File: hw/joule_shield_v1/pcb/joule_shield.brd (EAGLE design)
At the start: 60 x 40 mm, 138 parts, among them J1 MF-CON-MICROUSB-RIGHT, J4 USB_AUSB_A_SMT_RA, J5 JST-ZH5JST_ZH_SMT_VERT, J6 INTEL_JOULE_J6, J7 INTEL_JOULE_J7, J8 DM3ATDM3AT, SW1 MF-SW-TACT-4.2MM, SW2 MF-SW-TACT-4.2MM, SW3 MF-SW-TACT-4.2MM, U1 BQ25892PWQFN-24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

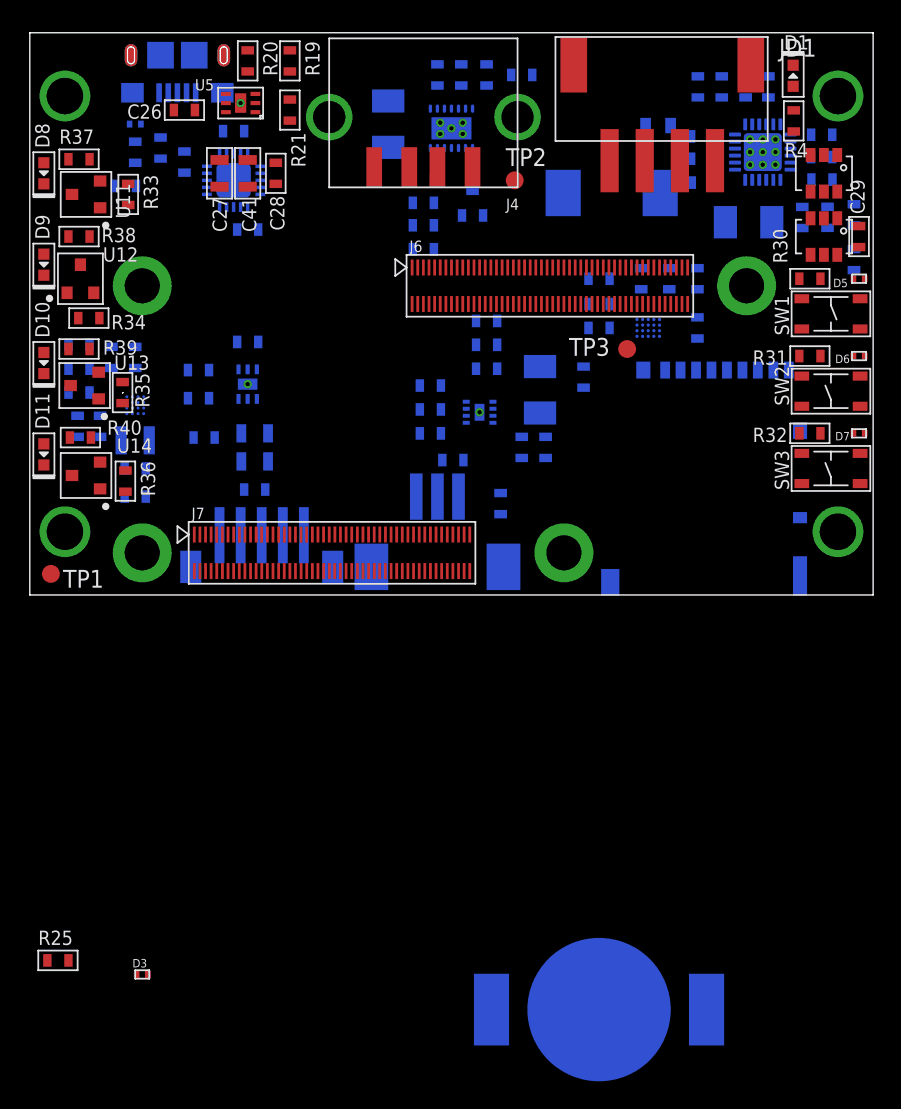
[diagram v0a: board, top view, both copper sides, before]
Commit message: joule shield: Put a sufficient keepout distance around m2.5 mounting holes.
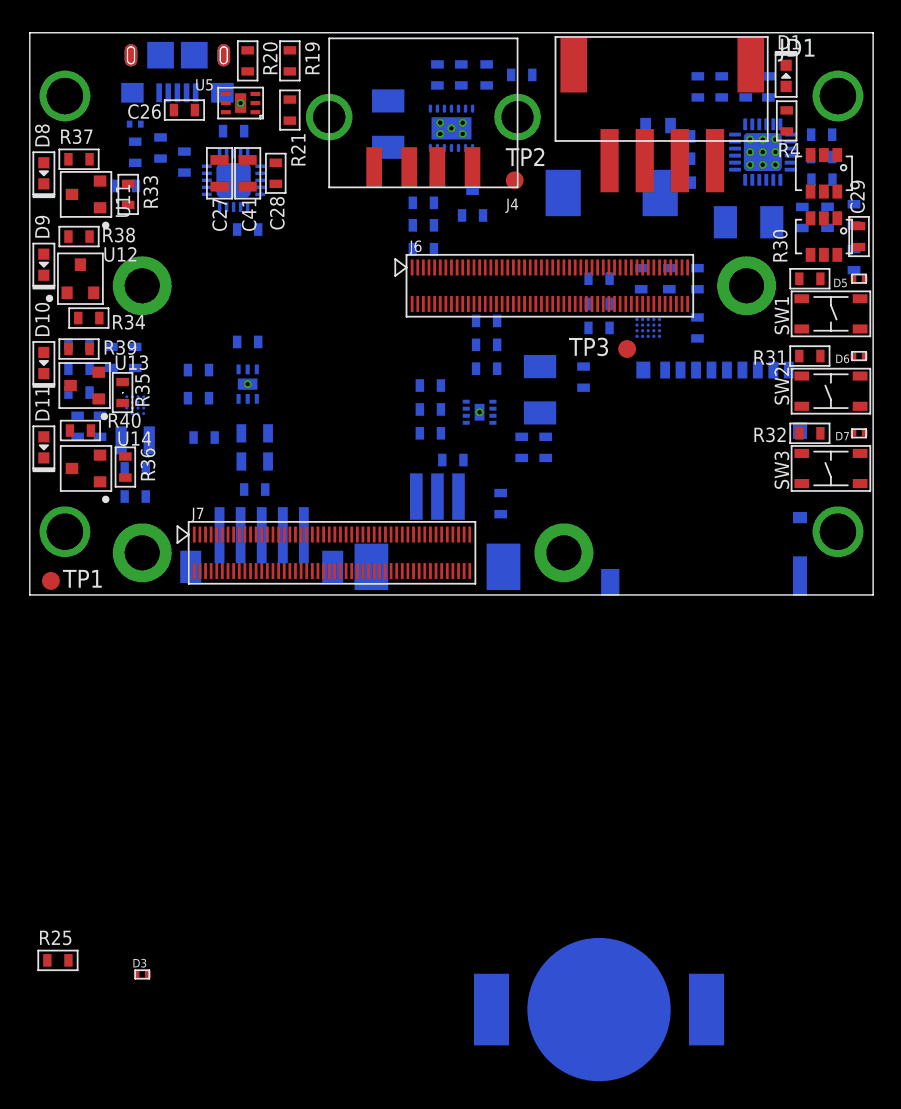
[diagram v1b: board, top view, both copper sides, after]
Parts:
- moved R36 1.00 mm to (6.80, 9.10)
- moved D1 0.50 mm to (53.8, 36.9)
- moved D11 0.50 mm to (1.00, 10.5)
- moved R4 0.50 mm to (53.9, 33.7)
- moved R40 0.50 mm to (3.60, 11.7)
- moved TP1 0.50 mm to (1.50, 1.00)
- moved U14 0.50 mm to (4.00, 9.00)
- flipped U$54 to the top

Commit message: joule shield: Switch to a smaller RTC battery and get everything on the board.
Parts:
- JRTC: value BK-916BK-916 -> BC-2009; device joule_shield:BK-916 -> joule_shield:BC-2009
- moved JRTC 53.9 mm to (19.2, 20.0), turned to 0 degrees
- moved D3 43.5 mm to (9.50, 16.5), flipped to the bottom, turned to 180 degrees
- moved R25 41.7 mm to (12.0, 14.5), flipped to the bottom, turned to 270 degrees
- moved C32 8.25 mm to (24.0, 9.50), turned to 270 degrees
- moved C30 8.14 mm to (10.0, 12.0), turned to 270 degrees
- moved R23 7.50 mm to (12.0, 8.50), turned to 90 degrees
- moved C42 6.02 mm to (22.0, 9.00), turned to 270 degrees
- moved R22 5.82 mm to (13.9, 8.50), turned to 90 degrees
- moved C12 5.76 mm to (5.50, 12.4)
- moved R11 5.72 mm to (4.90, 22.0)
- moved R8 5.68 mm to (3.30, 22.0)
- moved U2 5.59 mm to (5.00, 18.5)
- moved C11 5.39 mm to (5.50, 14.0)
- moved L2 5.39 mm to (5.50, 16.0)
- moved R24 5.22 mm to (16.8, 8.40), turned to 270 degrees
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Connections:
- net GND: now also JRTC.N1; no longer JRTC.2
- net N$30: now also JRTC.P1, JRTC.P2; no longer JRTC.1, JRTC.3

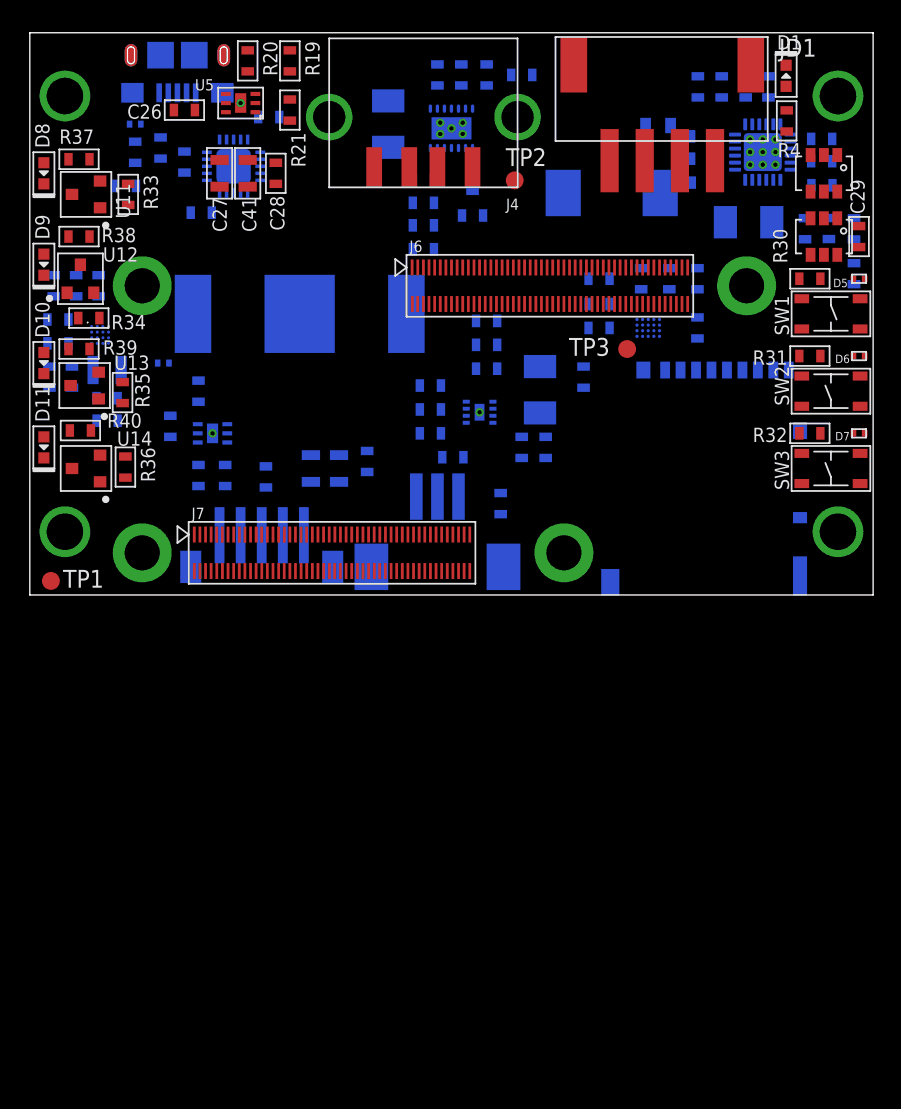
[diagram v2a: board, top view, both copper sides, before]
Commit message: joule_shield: Swap SD level converter for one with a 0.5mm BGA pitch so that there is at least one macrofab process which can route it. Further work on draft placement.  Everything is kinda on the board now.
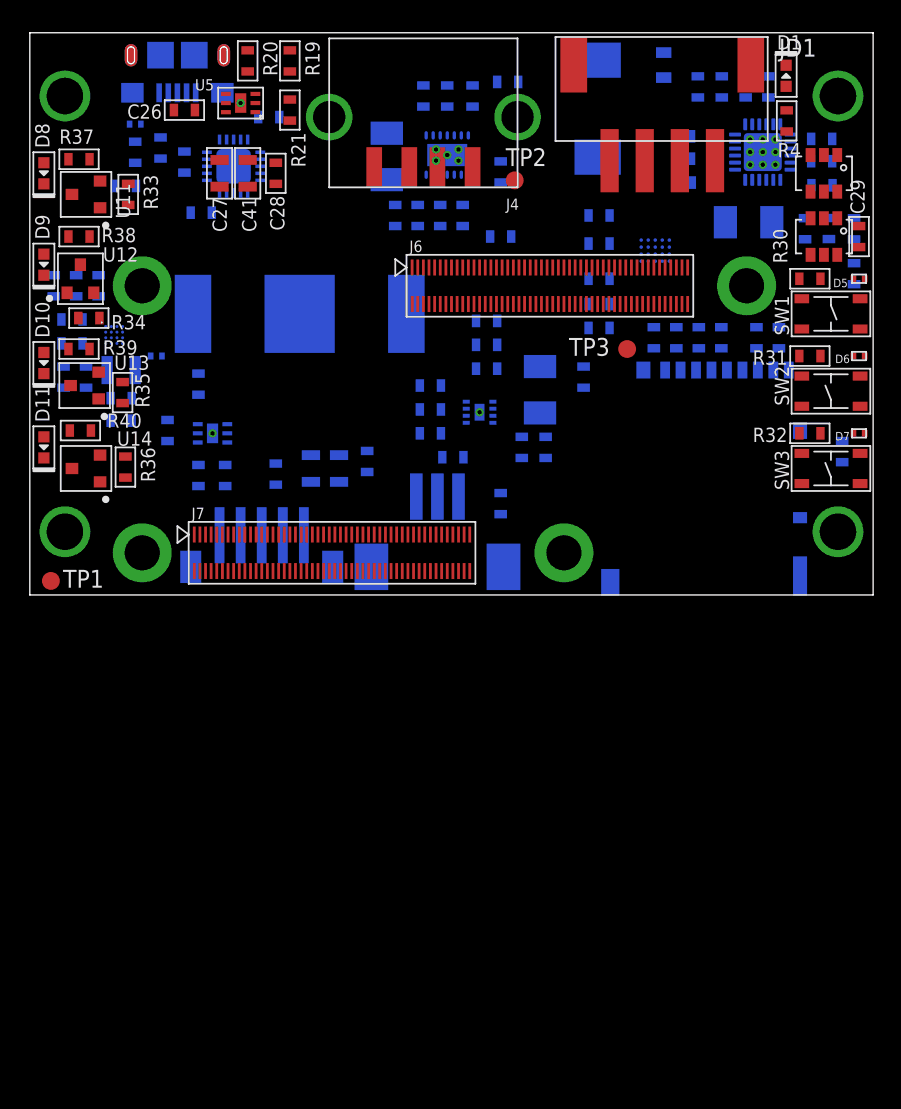
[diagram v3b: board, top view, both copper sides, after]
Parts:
- added R41, R42, R43, R44, R45: 100k, mf_passives:R0603
- U9: value TXS0206-29 -> SN74AVCA406L; device joule_shield:DSBGA20 -> joule_shield:S-PBGA-N20
- moved R26 16.0 mm to (57.8, 10.2), turned to 270 degrees
- moved C35 6.73 mm to (40.5, 27.0), turned to 0 degrees
- moved D2 6.08 mm to (40.4, 34.6), turned to 270 degrees
- moved U9 5.52 mm to (44.5, 24.5), turned to 0 degrees
- moved F1 4.32 mm to (45.1, 37.7), turned to 270 degrees
- moved FB2 3.91 mm to (40.5, 25.0), turned to 0 degrees
- moved C20 3.69 mm to (30.8, 27.0), turned to 270 degrees
- moved C17 3.20 mm to (26.0, 27.0), turned to 270 degrees
- moved R14 2.50 mm to (33.5, 25.5)
- moved L3 2.30 mm to (25.4, 31.2)
- moved C16 2.09 mm to (33.5, 30.1)
- moved U3 1.92 mm to (29.7, 31.3)
- moved C36 1.84 mm to (49.2, 18.3)
- moved C13 1.80 mm to (28.0, 35.5)
- moved C14 1.80 mm to (29.7, 35.5)
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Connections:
- removed net N$35: C36.P$1, J8.4, U9.B3
- removed net N$37: C34.P$1, C35.P$1, FB2.P$1, U9.B2
- removed net N$38: C33.P$1, FB1.P$2, U9.A2
- removed net N$40: J8.7, U9.D4
- new net N$69: J8.7, R45.P$2, U9.D2
- new net SDCARD_LVL_CMD_DIR: J6.90, U9.B5
- new net SDCARD_LVL_DAT_DIR: J6.67, U9.C1, U9.C5
- new net SDCARD_VCCA: C33.P$1, FB1.P$2, R26.P$1, U9.A5
- new net SDCARD_VCCB: C34.P$1, C35.P$1, C36.P$1, FB2.P$1, J8.4, R41.P$1, R42.P$1, R43.P$1, R44.P$1, R45.P$1, U9.D5
- net GND: now also U9.B3; no longer R26.P$2, U9.C2
- net N$41: now also R44.P$2, U9.D1; no longer U9.E4
- net N$42: now also R43.P$2, U9.C4; no longer U9.A4
- net N$43: now also R42.P$2, U9.D4; no longer U9.B4
- net N$44: now also R41.P$2, U9.C2; no longer U9.C4
- net SDCARD_CD: now also R26.P$2; no longer U9.A3
- net SDCARD_CLK: now also U9.A3; no longer U9.D2
- net SDCARD_CLK_FB: now also U9.A1; no longer U9.E2
- net SDCARD_CMD: now also U9.B1; no longer U9.C1
- net SDCARD_D0: now also U9.B2; no longer U9.D1
- net SDCARD_D1: now also U9.A2; no longer U9.E1
- net SDCARD_D2: now also U9.B4; no longer U9.A1
- net SDCARD_D3: now also U9.A4; no longer U9.B1
- net SDCARD_PWR_DOWN_N: no longer R26.P$1, U9.E3

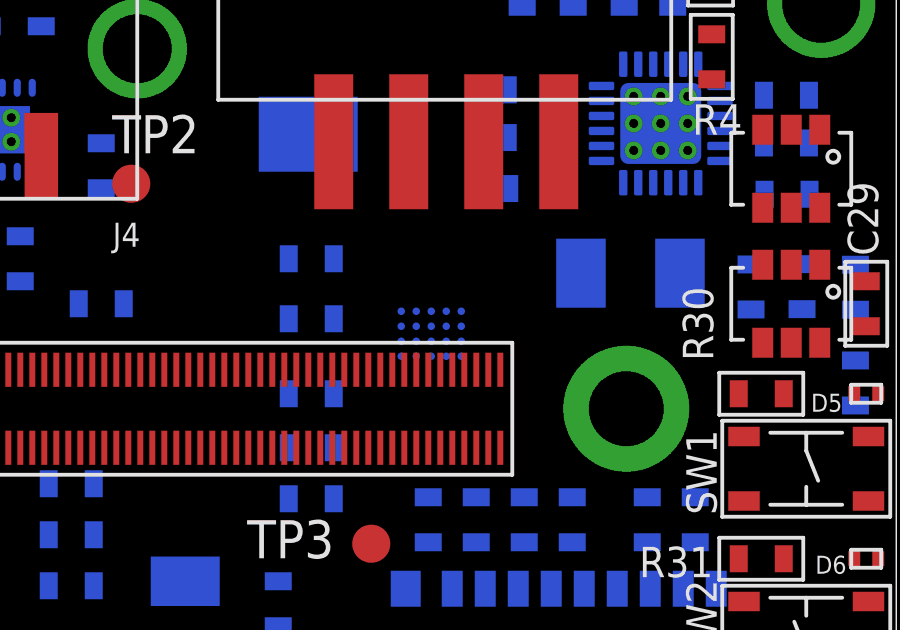
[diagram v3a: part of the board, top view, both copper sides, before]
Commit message: joule_shield: Switch to the MF extended DRU file.
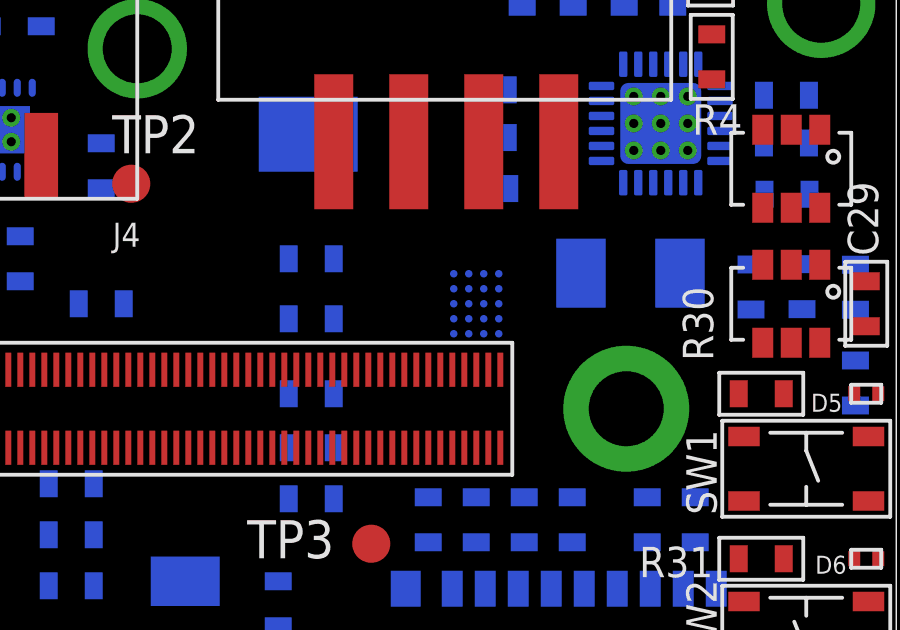
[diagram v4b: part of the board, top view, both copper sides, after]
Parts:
- moved U9 1.80 mm to (46.0, 25.5), turned to 270 degrees

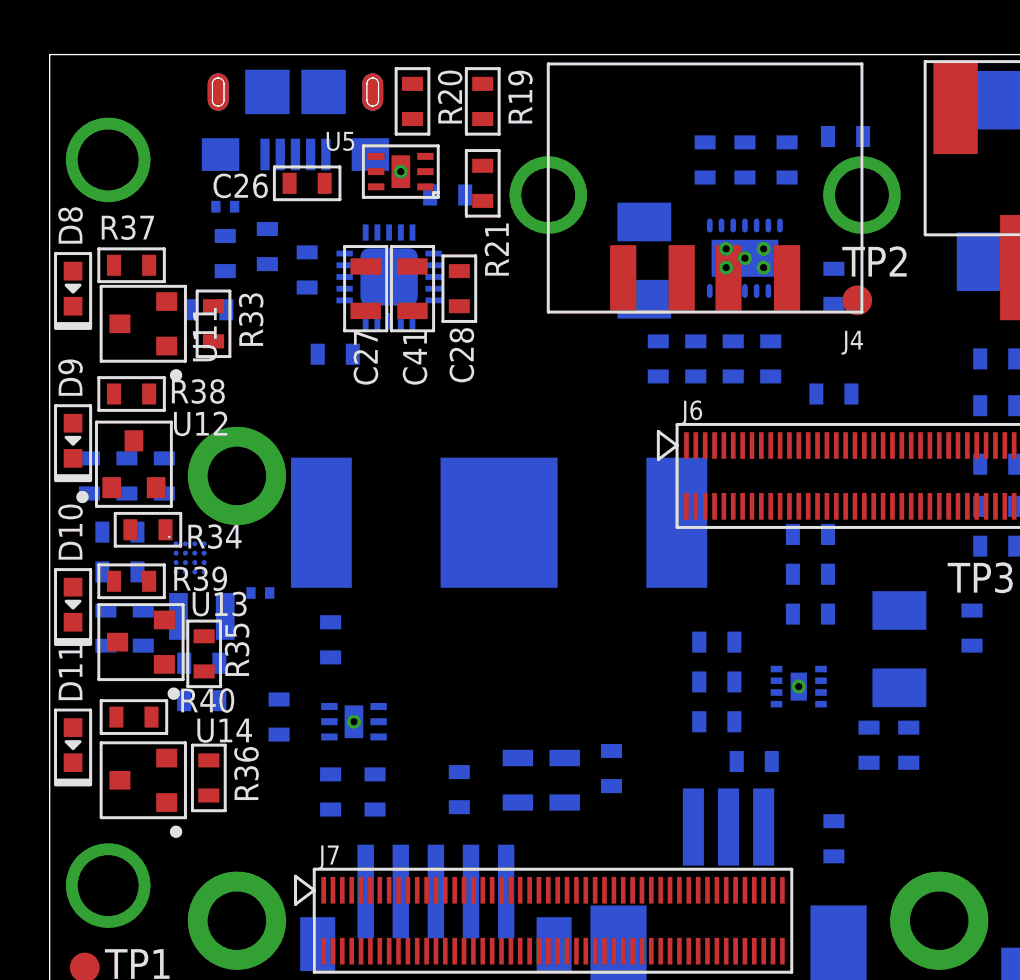
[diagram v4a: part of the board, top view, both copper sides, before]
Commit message: joule_shield: Connected up usb power switch enable and fault lines to GPIO pins.  Switched to smaller mosfets instead of MF house bipolars.
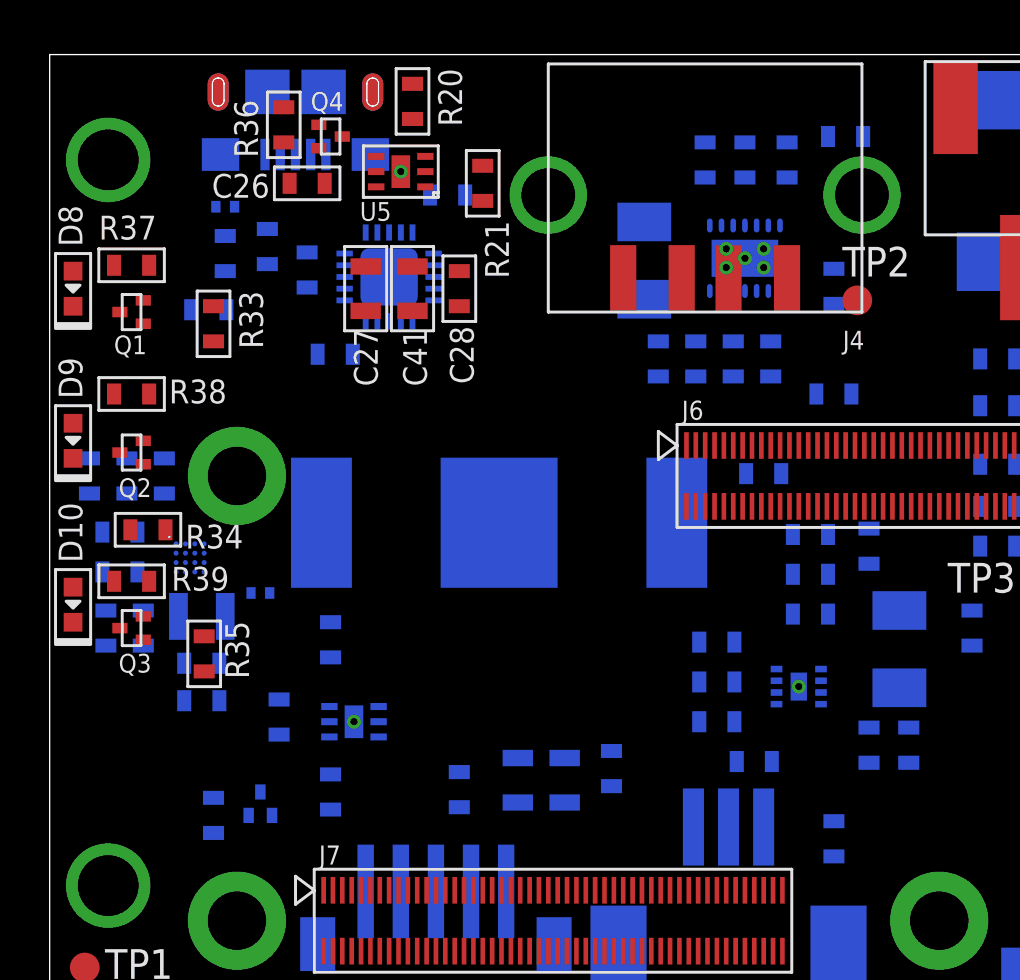
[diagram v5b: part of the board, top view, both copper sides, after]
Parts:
- removed D11: MF-LED-0603-GREEN, mf_leds:LED0603
- removed U11, U12, U13, U14: MF-DSC-SOT233-MMBT3904, mf_discrete_semiconductor:SOT-23-3
- added Q1, Q2, Q3, Q4, Q5: NFETEMT3F, joule_shield:EMT3F
- R36: value 1k -> 100k
- R40: value 470 -> 100k
- moved R36 28.1 mm to (10.0, 37.0)
- moved R19 25.2 mm to (35.0, 19.0), flipped to the bottom, turned to 90 degrees
- moved R22 21.5 mm to (30.5, 22.1), turned to 180 degrees
- moved R40 5.40 mm to (7.00, 7.50), flipped to the bottom, turned to 90 degrees
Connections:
- removed net N$22: R19.P$2, U5.3
- removed net N$32: R22.P$2, U6.3
- removed net N$55: D11.ANODE, R40.P$2
- removed net N$62: D11.CATHODE, U14.P$3
- removed net N$63: R33.P$2, U11.P$1
- removed net N$64: R34.P$2, U12.P$1
- removed net N$65: R35.P$2, U13.P$1
- removed net N$66: R36.P$2, U14.P$1
- new net ISH_GPIO_4: J6.29, Q5.1, R40.P$1
- new net ISH_GPIO_5: J6.38, R19.P$2, U5.3
- new net ISH_GPIO_6: J6.31, R22.P$2, U6.3
- net GND: now also Q1.2, Q2.2, Q3.2, Q4.2, Q5.2, R33.P$1, R34.P$1, R35.P$1, R36.P$2, R40.P$2; no longer U11.P$2, U12.P$2, U13.P$2, U14.P$2
- net ISH_GPIO_0: now also Q1.1, R33.P$2; no longer R33.P$1
- net ISH_GPIO_1: now also Q2.1, R34.P$2; no longer R34.P$1
- net ISH_GPIO_2: now also Q3.1, R35.P$2; no longer R35.P$1
- net ISH_GPIO_3: now also Q4.1
- net N$24: now also Q4.3
- net N$33: now also Q5.3
- net N$59: now also Q1.3; no longer U11.P$3
- net N$60: now also Q2.3; no longer U12.P$3
- net N$61: now also Q3.3; no longer U13.P$3
- net V5P0V: no longer R19.P$1, R22.P$1, R40.P$1
- net VDD1: now also R19.P$1, R22.P$1
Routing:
- added copper zone on layer 2, net GND
- added copper zone on layer 15, net VSYS
